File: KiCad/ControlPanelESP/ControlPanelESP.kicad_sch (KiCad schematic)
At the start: 20 parts

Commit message: initial version of PCB
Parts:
- added H1, H2, H3, H4: MountingHole_Pad, MountingHole:MountingHole_2.2mm_M2_DIN965_Pad, symbol Mechanical:MountingHole_Pad
- added J3, J6: Conn_01x04_Male, symbol Connector:Conn_01x04_Male
- added J4: Conn_01x03_Male, Connector_JST:JST_XH_B3B-XH-A_1x03_P2.50mm_Vertical, symbol Connector:Conn_01x03_Male
- added J5, J7: Conn_01x02_Male, Connector_JST:JST_XH_B2B-XH-A_1x02_P2.50mm_Vertical, symbol Connector:Conn_01x02_Male
- added K1: DIPxx-1Axx-11x, Lichtwecker:HF49FD-005-1H, symbol Relay:DIPxx-1Axx-11x
- added Q3, Q4, Q5: Q_NMOS_GSD, Package_TO_SOT_SMD:SOT-23, symbol Device:Q_NMOS_GSD
- added R10, R11, R5, R8: 10k, Resistor_SMD:R_0805_2012Metric_Pad1.20x1.40mm_HandSolder, symbol Device:R
- added R6: 4k7, Resistor_SMD:R_0805_2012Metric_Pad1.20x1.40mm_HandSolder, symbol Device:R
- added R7, R9: 1k, Resistor_SMD:R_0805_2012Metric_Pad1.20x1.40mm_HandSolder, symbol Device:R
- added U3: LTV-817, Package_DIP:DIP-4_W7.62mm, symbol Isolator:LTV-817
- D1: renamed from D?; footprint (none) -> LED_SMD:LED_0805_2012Metric_Pad1.15x1.40mm_HandSolder
- gave numbers to parts that had none: 19
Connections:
- net +5V: now also J3.4 (Pin_4), J4.2 (Pin_2), J6.4 (Pin_4), K1.6, R10.1, R5.1, R6.1, R7.1
- net GND: now also H1.1, H2.1, H3.1, H4.1, J3.1 (Pin_1), J6.1 (Pin_1), J6.2 (Pin_2), Q3.2 (S), Q4.2 (S), Q5.2 (S), R11.2, R8.2
- net BUTTON: now reaches U2.10 (IO25)
- net BUTTON: now also J6.3 (Pin_3), R10.2
- net DS18B20: now reaches U2.13 (IO14)
- net DS18B20: now also J3.3 (Pin_3), R6.2
- net FAN: now reaches U2.14 (IO12)
- net FAN: now also Q4.1 (G), R8.1
- net LED: now reaches U2.16 (IO13)
- net LED: now also Q3.1 (G), R5.2
- net Relay: now reaches U2.23 (IO15)
- net Relay: now also Q5.1 (G), R11.1
- net WS2812: now reaches U2.8 (IO32)
- net WS2812: now also J3.2 (Pin_2)
- new net: J4.1 (Pin_1), Q4.3 (D)
- new net: J5.1 (Pin_1), U3.3
- new net: J5.2 (Pin_2), R9.2
- new net: R7.2, U3.1
- new net: R9.1, U3.4
- new net: Q3.3 (D), U3.2
- new net: J7.1 (Pin_1), K1.1, K1.14
- new net: J7.2 (Pin_2), K1.7, K1.8
- new net: K1.2, Q5.3 (D)
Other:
- note added: "BUTTON"
- note added: "DS18B20 and WS2812B"
- note added: "DTR & RTS"
- note added: "FAN PWM"
- note added: "WAKE LED"
- moved on the sheet: Q1, Q2, R1, R2

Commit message: second version
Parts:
- added C8, C9: C_Polarized, Capacitor_THT:CP_Radial_D5.0mm_P2.00mm, symbol Device:C_Polarized
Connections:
- net +3V3: now also C9.1
- net +5V: now also C8.1
- net GND: now also C8.2, C9.2
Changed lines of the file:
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@@
   (junction (at 34.29 139.7) (diameter 0) (color 0 0 0 0)
   )
+  (junction (at 46.99 39.37) (diameter 0) (color 0 0 0 0)
+  )
   (junction (at 223.52 128.27) (diameter 0) (color 0 0 0 0)
   )
   (junction (at 210.82 54.61) (diameter 0) (color 0 0 0 0)
   )
+  (junction (at 69.85 39.37) (diameter 0) (color 0 0 0 0)
+  )
   (junction (at 60.96 182.88) (diameter 0) (color 0 0 0 0)
   )
@@
   (junction (at 139.7 176.53) (diameter 0) (color 0 0 0 0)
   )
+  (junction (at 38.1 30.48) (diameter 0) (color 0 0 0 0)
+  )
+  (junction (at 69.85 30.48) (diameter 0) (color 0 0 0 0)
+  )
   (junction (at 24.13 165.1) (diameter 0) (color 0 0 0 0)
   )
@@
     (stroke (width 0) (type default) (color 0 0 0 0))
   )
+  (wire (pts (xy 38.1 30.48) (xy 46.99 30.48))
+    (stroke (width 0) (type default) (color 0 0 0 0))
+  )
+  (wire (pts (xy 69.85 39.37) (xy 78.74 39.37))
+    (stroke (width 0) (type default) (color 0 0 0 0))
+  )
   (wire (pts (xy 46.99 125.73) (xy 46.99 129.54))
     (stroke (width 0) (type default) (color 0 0 0 0))
@@
     (stroke (width 0) (type default) (color 0 0 0 0))
   )
+  (wire (pts (xy 69.85 30.48) (xy 78.74 30.48))
+    (stroke (width 0) (type default) (color 0 0 0 0))
+  )
   (wire (pts (xy 97.79 175.26) (xy 97.79 167.64))
     (stroke (width 0) (type default) (color 0 0 0 0))
@@
     (stroke (width 0) (type default) (color 0 0 0 0))
   )
-  (wire (pts (xy 60.96 39.37) (xy 78.74 39.37))
+  (wire (pts (xy 60.96 39.37) (xy 69.85 39.37))
     (stroke (width 0) (type default) (color 0 0 0 0))
   )
@@
     (stroke (width 0) (type default) (color 0 0 0 0))
   )
-  (wire (pts (xy 68.58 30.48) (xy 78.74 30.48))
+  (wire (pts (xy 68.58 30.48) (xy 69.85 30.48))
     (stroke (width 0) (type default) (color 0 0 0 0))
   )
@@
     (stroke (width 0) (type default) (color 0 0 0 0))
   )
+  (wire (pts (xy 38.1 38.1) (xy 38.1 39.37))
+    (stroke (width 0) (type default) (color 0 0 0 0))
+  )
   (wire (pts (xy 210.82 54.61) (xy 210.82 44.45))
     (stroke (width 0) (type default) (color 0 0 0 0))
@@
     (stroke (width 0) (type default) (color 0 0 0 0))
   )
+  (wire (pts (xy 38.1 39.37) (xy 46.99 39.37))
+    (stroke (width 0) (type default) (color 0 0 0 0))
+  )
   (wire (pts (xy 218.44 128.27) (xy 223.52 128.27))
     (stroke (width 0) (type default) (color 0 0 0 0))
   )
-  (wire (pts (xy 26.67 30.48) (xy 46.99 30.48))
+  (wire (pts (xy 26.67 30.48) (xy 38.1 30.48))
     (stroke (width 0) (type default) (color 0 0 0 0))
   )
@@
   )
   (polyline (pts (xy 15.24 111.76) (xy 105.41 111.76))
+    (stroke (width 0) (type default) (color 0 0 0 0))
+  )
+  (wire (pts (xy 69.85 38.1) (xy 69.85 39.37))
     (stroke (width 0) (type default) (color 0 0 0 0))
   )
@@
     (pin "2")
   )
+  (symbol (lib_id "Device:C_Polarized") (at 69.85 34.29 0) (unit 1)
+    (in_bom yes) (on_board yes) (fields_autoplaced)
+    (property "Reference" "C9" (id 0) (at 72.771 32.4925 0)
+      (effects (font (size 1.27 1.27)) (justify left))
+    )
+    (property "Value" "C_Polarized" (id 1) (at 72.771 35.2676 0)
+      (effects (font (size 1.27 1.27)) (justify left))
+    )
+    (property "Footprint" "Capacitor_THT:CP_Radial_D5.0mm_P2.00mm" (id 2) (at 70.8152 38.1 0)
+      (effects (font (size 1.27 1.27)) hide)
+    )
+    (property "Datasheet" "~" (id 3) (at 69.85 34.29 0)
+      (effects (font (size 1.27 1.27)) hide)
+    )
+    (pin "1")
+    (pin "2")
+  )
   (symbol (lib_id "power:+5V") (at 231.14 106.68 0) (unit 1)
     (in_bom yes) (on_board yes) (fields_autoplaced)
@@
     (pin "1")
   )
+  (symbol (lib_id "Device:C_Polarized") (at 38.1 34.29 0) (unit 1)
+    (in_bom yes) (on_board yes) (fields_autoplaced)
+    (property "Reference" "C8" (id 0) (at 41.021 32.4925 0)
+      (effects (font (size 1.27 1.27)) (justify left))
+    )
+    (property "Value" "C_Polarized" (id 1) (at 41.021 35.2676 0)
+      (effects (font (size 1.27 1.27)) (justify left))
+    )
+    (property "Footprint" "Capacitor_THT:CP_Radial_D5.0mm_P2.00mm" (id 2) (at 39.0652 38.1 0)
+      (effects (font (size 1.27 1.27)) hide)
+    )
+    (property "Datasheet" "~" (id 3) (at 38.1 34.29 0)
+      (effects (font (size 1.27 1.27)) hide)
+    )
+    (pin "1")
+    (pin "2")
+  )
   (symbol (lib_id "Device:C") (at 46.99 35.56 0) (unit 1)
     (in_bom yes) (on_board yes) (fields_autoplaced)
@@
       (reference "C7") (unit 1) (value "100n") (footprint "Capacitor_SMD:C_0805_2012Metric_Pad1.18x1.45mm_HandSolder")
     )
+    (path "/fb12d38d-9b26-4e6c-9a22-280965560e28"
+      (reference "C8") (unit 1) (value "C_Polarized") (footprint "Capacitor_THT:CP_Radial_D5.0mm_P2.00mm")
+    )
+    (path "/cd0e1ec8-5612-4244-a876-838286424de9"
+      (reference "C9") (unit 1) (value "C_Polarized") (footprint "Capacitor_THT:CP_Radial_D5.0mm_P2.00mm")
+    )
     (path "/3cacc5b5-0b9a-41df-a427-24c30f1eb6f8"

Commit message: V2.0 of PCB
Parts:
- removed D1: LED, LED_SMD:LED_0805_2012Metric_Pad1.15x1.40mm_HandSolder, symbol Device:LED
- removed J2: Conn_01x06_Male, Connector_JST:JST_XH_B6B-XH-A_1x06_P2.50mm_Vertical, symbol Connector:Conn_01x06_Male
- removed J4: Conn_01x03_Male, Connector_JST:JST_XH_B3B-XH-A_1x03_P2.50mm_Vertical, symbol Connector:Conn_01x03_Male
- removed J6: Conn_01x04_Male, symbol Connector:Conn_01x04_Male
- removed J7: Conn_01x02_Male, Connector_JST:JST_XH_B2B-XH-A_1x02_P2.50mm_Vertical, symbol Connector:Conn_01x02_Male
- removed Q1, Q2: Q_NPN_BEC, Package_TO_SOT_SMD:SOT-23, symbol Device:Q_NPN_BEC
- added H5: MountingHole_Pad, MountingHole:MountingHole_2.2mm_M2_DIN965_Pad, symbol Mechanical:MountingHole_Pad
- added IC1: MCP3221A6T-E_OT, SOT95P280X145-5N, symbol SamacSys_Parts:MCP3221A6T-E_OT
- added J2: Conn_01x04_Male, Connector_PinHeader_2.54mm:PinHeader_1x04_P2.54mm_Vertical, symbol Connector:Conn_01x04_Male
- added J4: Conn_01x02_Male, Connector_PinHeader_2.54mm:PinHeader_1x02_P2.54mm_Vertical, symbol Connector:Conn_01x02_Male
- added J6: Conn_01x03_Male, Connector_PinHeader_2.54mm:PinHeader_1x03_P2.54mm_Vertical, symbol Connector:Conn_01x03_Male
- added J7: 2086-3122, Lichtwecker:2086-3122, symbol Lichtwecker_Symbols:2086-3122
- added R12: 4k7, Resistor_SMD:R_0805_2012Metric_Pad1.20x1.40mm_HandSolder, symbol Device:R
- added U4: LM4040DIM3X-4.1, Package_TO_SOT_SMD:SOT-23, symbol Lichtwecker_Symbols:LM4040DIM3X-4.1
- J1, J5: footprint Connector_JST:JST_XH_B2B-XH-A_1x02_P2.50mm_Vertical -> Connector_PinHeader_2.54mm:PinHeader_1x02_P2.54mm_Vertical
- J3: footprint (none) -> Connector_PinHeader_2.54mm:PinHeader_1x04_P2.54mm_Vertical
- R2: value 10k -> 1k
- R3: value 1k -> 4k7
- R6: value 4k7 -> 5.1k
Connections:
- net DTR is gone; now on net +3V3: R1.1
- net +3V3: now also R12.1
- net +5V: now also R2.1, J2.1 (Pin_1), J4.2 (Pin_2), J6.3 (Pin_3)
- net BUTTON: now also J6.2 (Pin_2)
- net GND: now also IC1.2 (VSS), J2.2 (Pin_2), J6.1 (Pin_1), U4.2 (A); no longer H1.1, H2.1, H3.1, H4.1
- net IO0: now also R1.2
- net RX_ESP32: now also J2.3 (Pin_3)
- net TX_ESP32: now also J2.4 (Pin_4)
- net at Q4.3 (D): now also J4.1 (Pin_1)
- net SDA: now reaches U2.33 (IO21)
- net SDA: now also R3.2, IC1.4 (SDA)
- net SCL: now reaches U2.36 (IO22)
- net SCL: now also IC1.5 (SCL), R12.2
- net 230V1: now reaches K1.1, K1.14
- net 230V1: now also J7.2
- net 230V: now reaches K1.7, K1.8
- net 230V: now also J7.1
- net DS18B20 renamed TEMPSENSOR
- net TEMPSENSOR: now also IC1.3 (AIN); no longer U2.13 (IO14)
- net RTS: no longer names the net of R2.2
- net RTS: now also IC1.1 (VDD), U4.1 (K)
- no-connect marks 0 -> 27
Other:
- note removed: "DTR & RTS"
- moved on the sheet: Q5, R11

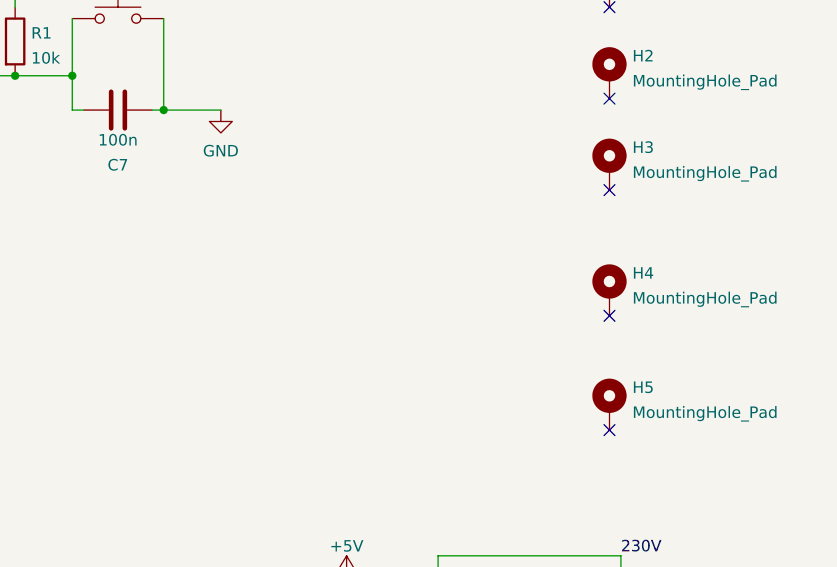
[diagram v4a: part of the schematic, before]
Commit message: add: OLED Display Connector, some markers
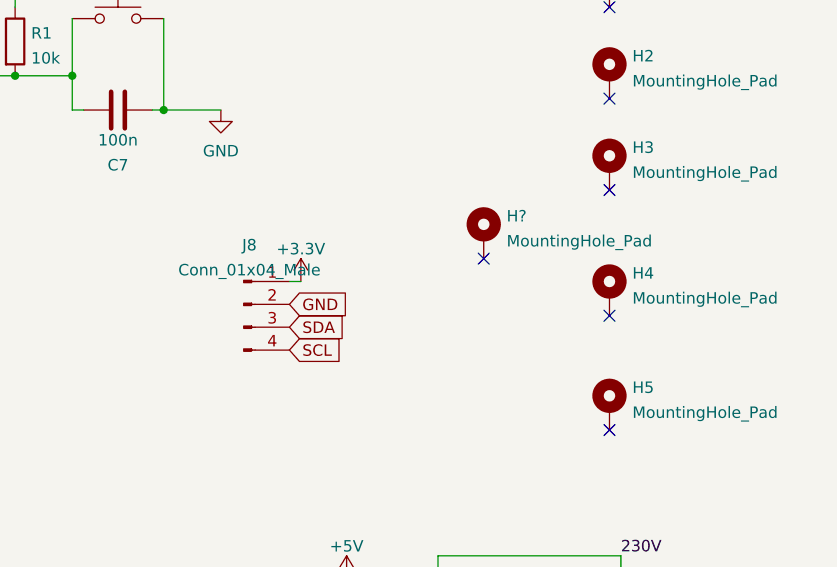
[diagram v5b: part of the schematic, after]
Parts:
- added H?: MountingHole_Pad, MountingHole:MountingHole_2.2mm_M2_DIN965_Pad, symbol Mechanical:MountingHole_Pad
- added J8: Conn_01x04_Male, Connector_PinHeader_2.54mm:PinHeader_1x04_P2.54mm_Vertical, symbol Connector:Conn_01x04_Male
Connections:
- net +3V3: now also J8.1 (Pin_1)
- net GND: now also J8.2 (Pin_2)
- net SCL: now also J8.4 (Pin_4)
- net SDA: now also J8.3 (Pin_3)
- no-connect marks 27 -> 28
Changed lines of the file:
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@@
   (no_connect (at 180.34 104.14))
   (no_connect (at 260.35 63.5))
+  (no_connect (at 246.38 71.12))
   (no_connect (at 260.35 53.34))
   (no_connect (at 260.35 43.18))
   (no_connect (at 260.35 77.47))
   (no_connect (at 260.35 90.17))
+  (wire (pts (xy 224.79 73.66) (xy 226.06 73.66))
+    (stroke (width 0) (type default) (color 0 0 0 0))
+  )
   (wire (pts (xy 135.89 132.08) (xy 139.7 132.08))
     (stroke (width 0) (type default) (color 0 0 0 0))
@@
     (effects (font (size 1.27 1.27)) (justify left))
     (property "Intersheet References" "${INTERSHEET_REFS}" (id 0) (at 192.2479 58.3406 0)
+      (effects (font (size 1.27 1.27)) (justify left) hide)
+    )
+  )
+  (global_label "SDA" (shape input) (at 224.79 78.74 0) (fields_autoplaced)
+    (effects (font (size 1.27 1.27)) (justify left))
+    (property "Intersheet References" "${INTERSHEET_REFS}" (id 0) (at 230.7712 78.6606 0)
+      (effects (font (size 1.27 1.27)) (justify left) hide)
+    )
+  )
+  (global_label "SCL" (shape input) (at 224.79 81.28 0) (fields_autoplaced)
+    (effects (font (size 1.27 1.27)) (justify left))
+    (property "Intersheet References" "${INTERSHEET_REFS}" (id 0) (at 230.7107 81.2006 0)
+      (effects (font (size 1.27 1.27)) (justify left) hide)
+    )
+  )
+  (global_label "GND" (shape input) (at 224.79 76.2 0) (fields_autoplaced)
+    (effects (font (size 1.27 1.27)) (justify left))
+    (property "Intersheet References" "${INTERSHEET_REFS}" (id 0) (at 231.0736 76.1206 0)
       (effects (font (size 1.27 1.27)) (justify left) hide)
     )
@@
     (pin "3")
   )
+  (symbol (lib_id "power:+3.3V") (at 226.06 73.66 0) (unit 1)
+    (in_bom yes) (on_board yes) (fields_autoplaced)
+    (property "Reference" "#PWR022" (id 0) (at 226.06 77.47 0)
+      (effects (font (size 1.27 1.27)) hide)
+    )
+    (property "Value" "+3.3V" (id 1) (at 226.06 70.0555 0))
+    (property "Footprint" "" (id 2) (at 226.06 73.66 0)
+      (effects (font (size 1.27 1.27)) hide)
+    )
+    (property "Datasheet" "" (id 3) (at 226.06 73.66 0)
+      (effects (font (size 1.27 1.27)) hide)
+    )
+    (pin "1")
+  )
   (symbol (lib_id "Switch:SW_Push") (at 205.74 44.45 0) (unit 1)
     (in_bom yes) (on_board yes) (fields_autoplaced)
@@
     (pin "2")
   )
+  (symbol (lib_id "Connector:Conn_01x04_Male") (at 219.71 76.2 0) (unit 1)
+    (in_bom yes) (on_board yes) (fields_autoplaced)
+    (property "Reference" "J8" (id 0) (at 220.345 69.6173 0))
+    (property "Value" "Conn_01x04_Male" (id 1) (at 220.345 72.3924 0))
+    (property "Footprint" "Connector_PinHeader_2.54mm:PinHeader_1x04_P2.54mm_Vertical" (id 2) (at 219.71 76.2 0)
+      (effects (font (size 1.27 1.27)) hide)
+    )
+    (property "Datasheet" "~" (id 3) (at 219.71 76.2 0)
+      (effects (font (size 1.27 1.27)) hide)
+    )
+    (pin "1")
+    (pin "2")
+    (pin "3")
+    (pin "4")
+  )
+  (symbol (lib_id "Mechanical:MountingHole_Pad") (at 246.38 68.58 0) (unit 1)
+    (in_bom yes) (on_board yes) (fields_autoplaced)
+    (property "Reference" "H?" (id 0) (at 248.92 66.4015 0)
+      (effects (font (size 1.27 1.27)) (justify left))
+    )
+    (property "Value" "MountingHole_Pad" (id 1) (at 248.92 69.1766 0)
+      (effects (font (size 1.27 1.27)) (justify left))
+    )
+    (property "Footprint" "MountingHole:MountingHole_2.2mm_M2_DIN965_Pad" (id 2) (at 246.38 68.58 0)
+      (effects (font (size 1.27 1.27)) hide)
+    )
+    (property "Datasheet" "~" (id 3) (at 246.38 68.58 0)
+      (effects (font (size 1.27 1.27)) hide)
+    )
+    (pin "1")
+  )
   (symbol (lib_id "power:GND") (at 107.95 62.23 0) (unit 1)
     (in_bom yes) (on_board yes) (fields_autoplaced)
@@
       (reference "#PWR021") (unit 1) (value "GND") (footprint "")
     )
+    (path "/ea58ebf5-6634-4ba8-8ed8-7f30f95d50b5"
+      (reference "#PWR022") (unit 1) (value "+3.3V") (footprint "")
+    )
     (path "/0cbcfd83-688e-47de-832c-610fdda040b9"
       (reference "#PWR026") (unit 1) (value "GND") (footprint "")
@@
       (reference "H5") (unit 1) (value "MountingHole_Pad") (footprint "MountingHole:MountingHole_2.2mm_M2_DIN965_Pad")
     )
+    (path "/f4136865-99c6-4217-9ef5-1189af92b8f7"
+      (reference "H?") (unit 1) (value "MountingHole_Pad") (footprint "MountingHole:MountingHole_2.2mm_M2_DIN965_Pad")
+    )
     (path "/4969196e-6305-4977-8756-05f46d7c9444"
       (reference "IC1") (unit 1) (value "MCP3221A6T-E_OT") (footprint "SOT95P280X145-5N")
@@
       (reference "J7") (unit 1) (value "2086-3122") (footprint "Lichtwecker:2086-3122")
     )
+    (path "/f3221d7d-1736-4b0b-9b3b-6e6333b33399"
+      (reference "J8") (unit 1) (value "Conn_01x04_Male") (footprint "Connector_PinHeader_2.54mm:PinHeader_1x04_P2.54mm_Vertical")
+    )
     (path "/af34f5bd-9c3b-44b4-99ba-829473dbca73"

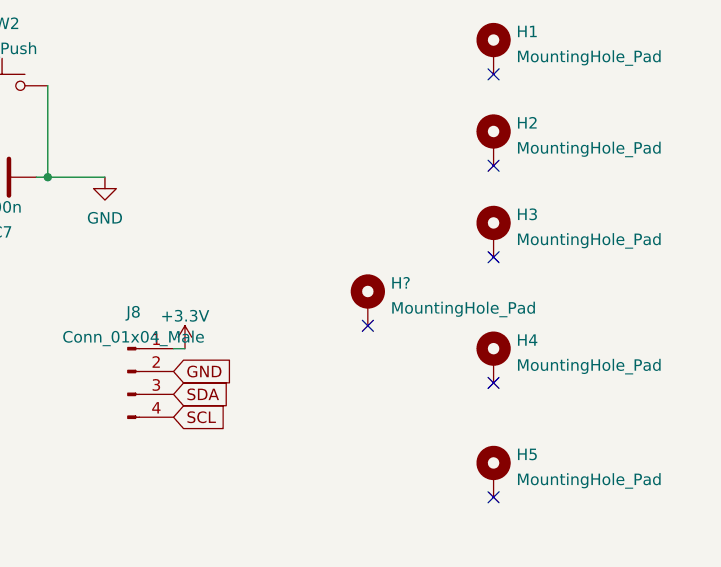
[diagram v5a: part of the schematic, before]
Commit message: add: OLED Display Header
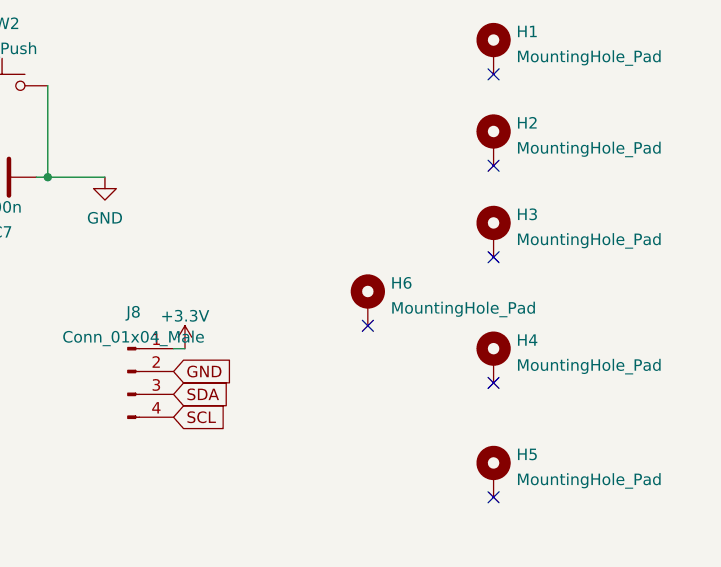
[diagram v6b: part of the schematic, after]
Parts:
- gave numbers to parts that had none: 1
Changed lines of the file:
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@@
   (symbol (lib_id "Mechanical:MountingHole_Pad") (at 246.38 68.58 0) (unit 1)
     (in_bom yes) (on_board yes) (fields_autoplaced)
-    (property "Reference" "H?" (id 0) (at 248.92 66.4015 0)
+    (property "Reference" "H6" (id 0) (at 248.92 66.4015 0)
       (effects (font (size 1.27 1.27)) (justify left))
     )
@@
     )
     (path "/f4136865-99c6-4217-9ef5-1189af92b8f7"
-      (reference "H?") (unit 1) (value "MountingHole_Pad") (footprint "MountingHole:MountingHole_2.2mm_M2_DIN965_Pad")
+      (reference "H6") (unit 1) (value "MountingHole_Pad") (footprint "MountingHole:MountingHole_2.2mm_M2_DIN965_Pad")
     )
     (path "/4969196e-6305-4977-8756-05f46d7c9444"

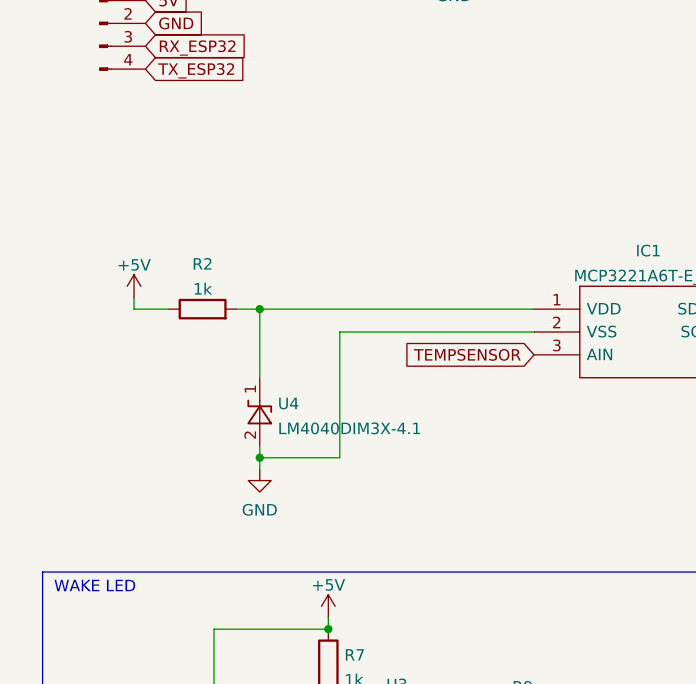
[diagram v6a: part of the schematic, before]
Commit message: ch: MCP1541 as voltage reference for ADC
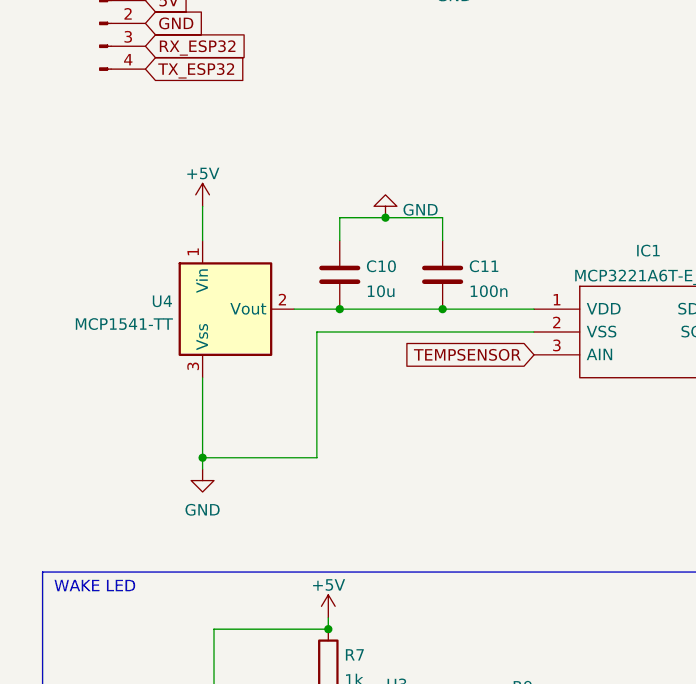
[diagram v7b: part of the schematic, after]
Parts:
- removed R2: 1k, Resistor_SMD:R_0805_2012Metric_Pad1.20x1.40mm_HandSolder, symbol Device:R
- removed U4: LM4040DIM3X-4.1, Package_TO_SOT_SMD:SOT-23, symbol Lichtwecker_Symbols:LM4040DIM3X-4.1
- added C10: 10u, Capacitor_SMD:C_0805_2012Metric_Pad1.18x1.45mm_HandSolder, symbol Device:C
- added C11: 100n, Capacitor_SMD:C_0805_2012Metric_Pad1.18x1.45mm_HandSolder, symbol Device:C
- added U4: MCP1541-TT, Package_TO_SOT_SMD:SOT-23, symbol Reference_Voltage:MCP1541-TT
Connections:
- net +5V: now also U4.1 (Vin)
- net GND: now also C10.2, C11.2, U4.3 (Vss)
- net at IC1.1 (VDD): now also C10.1, C11.1, U4.2 (Vout)
